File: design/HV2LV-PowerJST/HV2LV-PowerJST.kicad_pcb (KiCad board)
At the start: 2 copper layers, 50 x 17.5 mm, 9 parts, among them J1 S2B-PH-SM4-TB_LF__SN_, J2 S2B-PH-SM4-TB_LF__SN_, U1 AMS1117-3.3

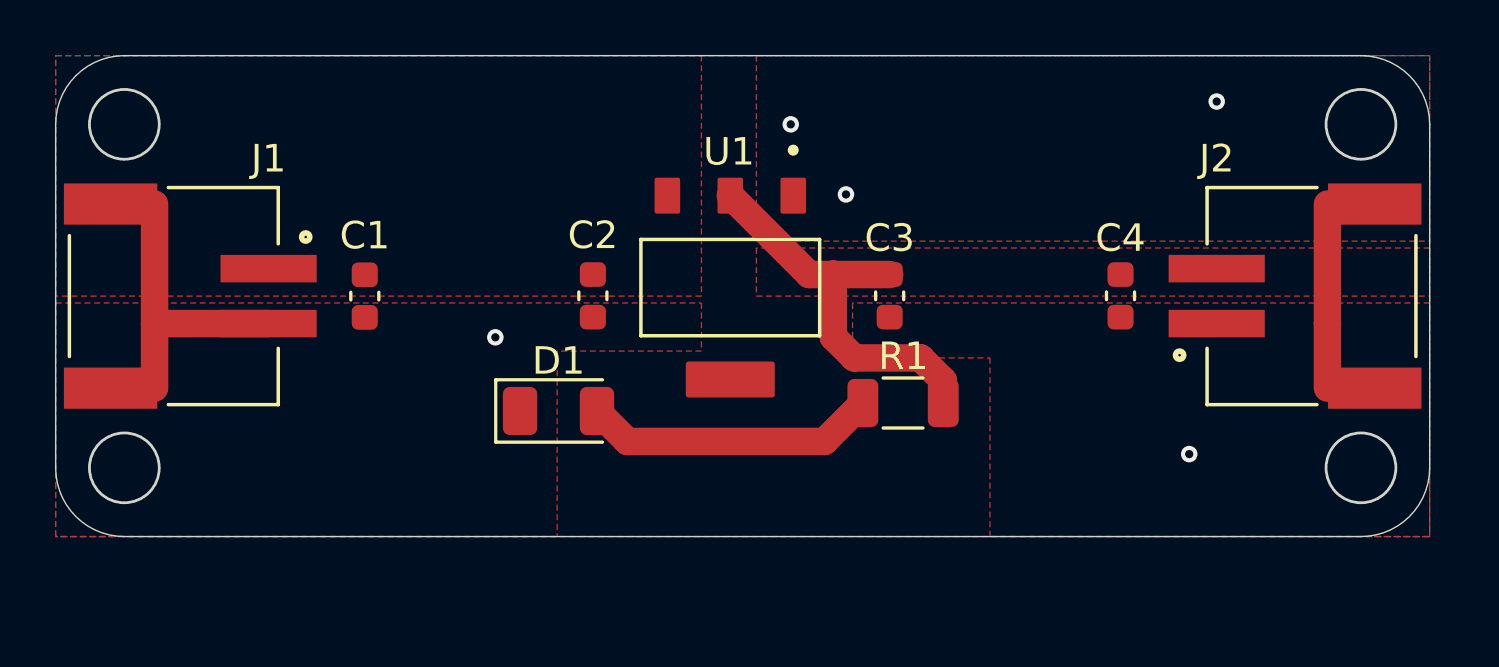
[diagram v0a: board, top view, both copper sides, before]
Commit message: best adaptation to adafruit swirly grill
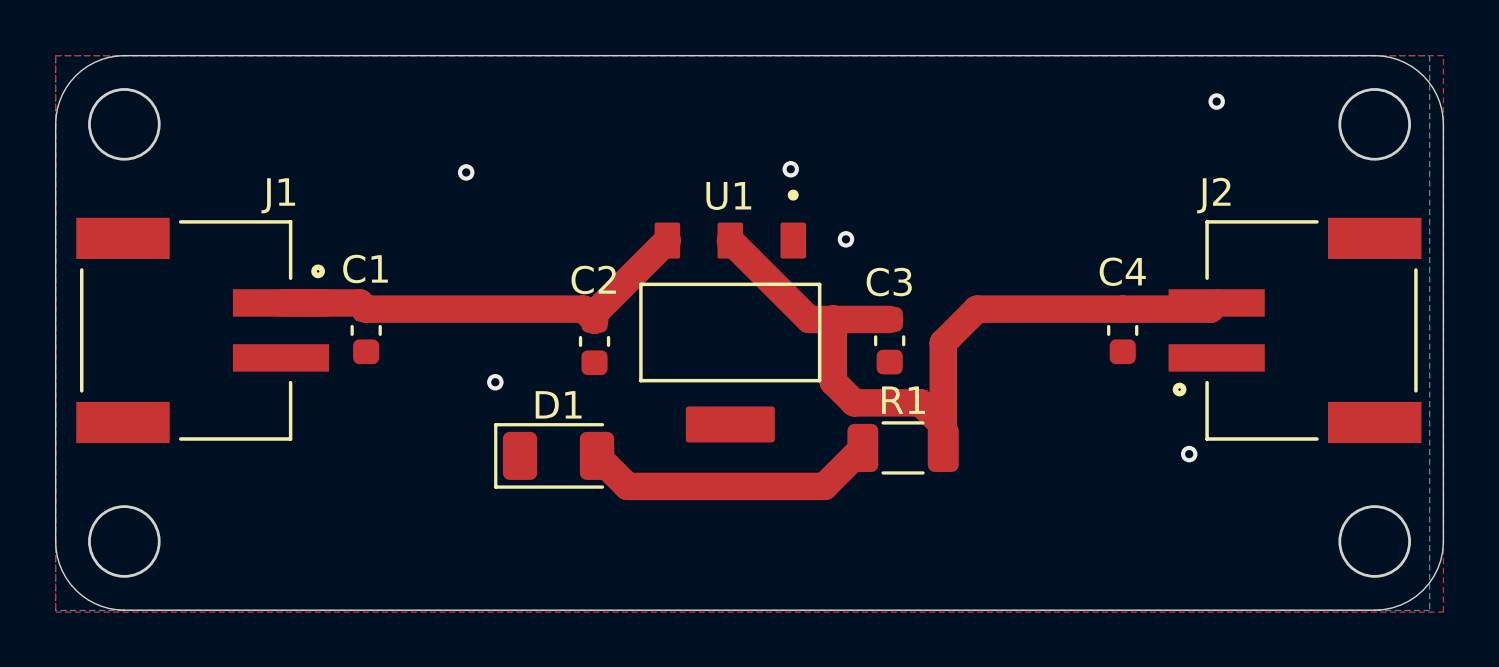
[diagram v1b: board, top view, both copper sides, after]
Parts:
- moved C2 1.66 mm to (39.6, 30.4)
- moved C3 1.64 mm to (50.4, 30.4)
- moved D1 1.63 mm to (38.3, 34.6)
- moved R1 1.63 mm to (50.8, 34.3)
- moved U1 1.63 mm to (44.5, 30.1)
- moved J1 1.33 mm to (28.2, 30.0)
- moved C4 1.26 mm to (58.8, 30.0)
- moved C1 1.25 mm to (31.3, 30.0)
- moved J2 1.25 mm to (62.2, 30.0)
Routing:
- net GND: track 17.6 -> 0.00 mm, vias 5 -> 6
- net Vin: track 0.00 -> 15.7 mm
- net Vout: track 14.8 -> 29.1 mm
- removed copper zone on F.Cu, net Vin
- removed copper zone on F.Cu, net Vout
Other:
- board size 50 x 17.5 mm -> 50.5 x 20.2 mm
